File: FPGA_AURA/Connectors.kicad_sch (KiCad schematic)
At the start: 4 parts, among them J1 TF-CARD_H1.8, J2 532617004, J3 532617007, J4 532617004

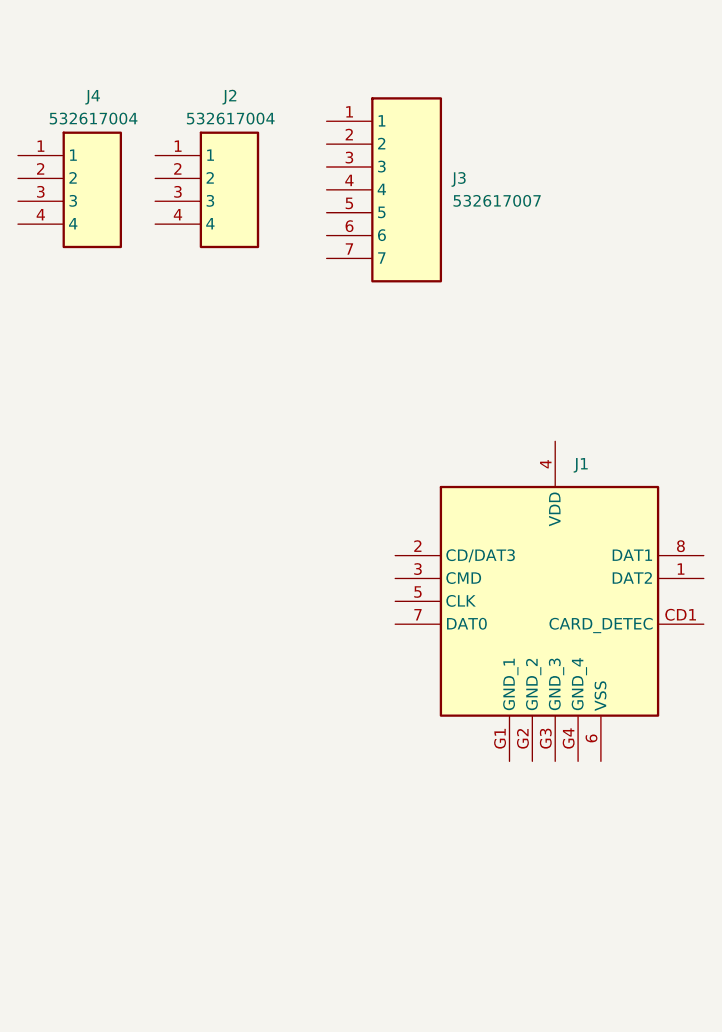
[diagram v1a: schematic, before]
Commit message: Changing stackup to 10 layers and connectors change
Development has been slow due to SI concerns with 8 layers so changing the layer count to 10 will simplify design. The picoblade/SD connector(s) are large and not high speed, so a high speed mezzanine will be used to go to a daughter board with the picoblade connectors and SD card, or other devices/protocols e.g. ADCs, COAX, IMUs, etc.
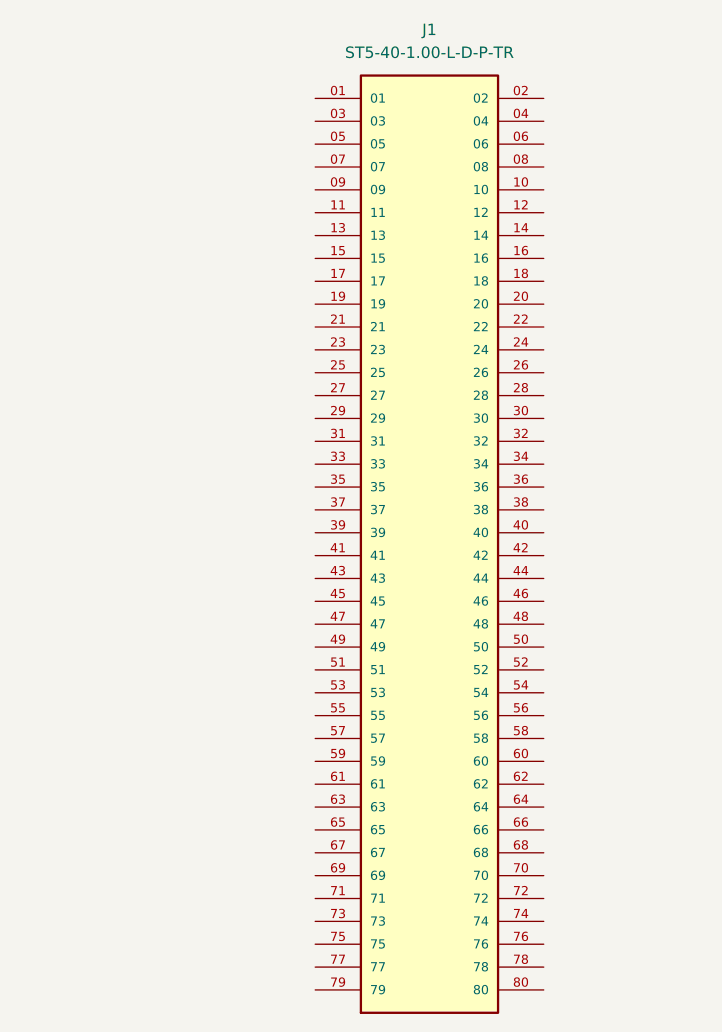
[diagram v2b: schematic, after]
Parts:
- removed J1: TF-CARD_H1.8, TF-CARD_H1_8:TFCARDH18, symbol TF-CARD_H1_8:TF-CARD_H1.8
- removed J2, J4: 532617004, 532617004:532617004, symbol 532617004:532617004
- removed J3: 532617007, 532617007, symbol 532617007:532617007
- added J1: ST5-40-1.00-L-D-P-TR, ST5-40-1.00-L-D-P-TR:ST5-40-1.00-L-D-P-TR, symbol ST5-40-1.00-L-D-P-TR:ST5-40-1.00-L-D-P-TR
